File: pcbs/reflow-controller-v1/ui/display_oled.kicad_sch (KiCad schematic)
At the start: 3 parts

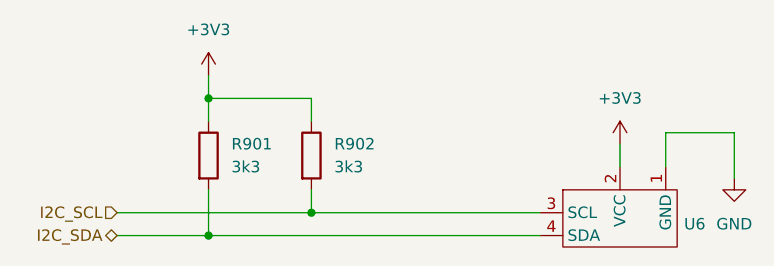
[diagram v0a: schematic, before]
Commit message: split pcbs into two for safety
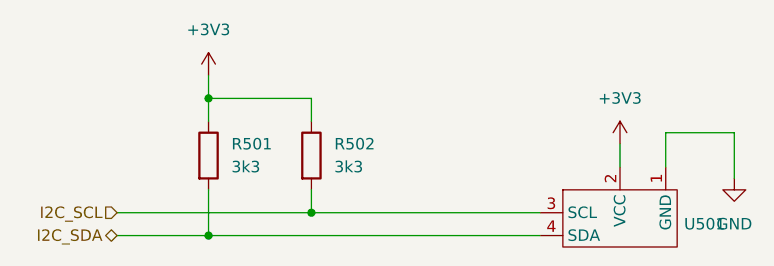
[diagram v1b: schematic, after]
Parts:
- renumbered R901 to R501, R902 to R502, U6 to U501
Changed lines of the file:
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@@
 (kicad_sch
-	(version 20231120)
+	(version 20250114)
 	(generator "eeschema")
-	(generator_version "8.0")
+	(generator_version "9.0")
 	(paper "A4")
 	(junction
@@
 		(shape input)
 		(at 91.44 88.9 180)
-		(fields_autoplaced yes)
 		(effects
 			(font
@@
 		(shape bidirectional)
 		(at 91.44 91.44 180)
-		(fields_autoplaced yes)
 		(effects
 			(font
@@
 		(dnp no)
 		(fields_autoplaced yes)
-		(property "Reference" "#PWR0903"
+		(property "Reference" "#PWR0503"
 			(at 160.02 91.44 0)
 			(effects
@@
 		)
 		(instances
-			(project "reflow-controller-v1"
-				(path "/843848ae-bf49-42cb-8f8b-76790d2e568d/28d32604-417d-4cd4-a8ef-2fae619450e6"
-					(reference "#PWR0903")
-					(unit 1)
-				)
-				(path "/843848ae-bf49-42cb-8f8b-76790d2e568d/41c2d982-496b-4922-a077-a2a7f833416c"
-					(reference "#PWR0803")
-					(unit 1)
-				)
-			)
-			(project "controller_v1"
-				(path "/c1daf800-73ea-4b6c-aa60-e9f4e3094257/1880ae86-b315-43a9-9217-9492e81597b0"
-					(reference "#PWR0403")
-					(unit 1)
-				)
-				(path "/c1daf800-73ea-4b6c-aa60-e9f4e3094257/4f03f492-0b54-42f8-83e4-aaa576a1d068"
-					(reference "#PWR0303")
-					(unit 1)
-				)
-				(path "/c1daf800-73ea-4b6c-aa60-e9f4e3094257/d31388c9-964a-4783-beb1-0c9e163732c0"
-					(reference "#PWR0203")
+			(project "ui"
+				(path "/2ced3b3e-2fc8-4776-88d1-4bcb3cd16514/6487fe46-90c2-4d94-907f-d4fbc81ee4e4"
+					(reference "#PWR0503")
+					(unit 1)
+				)
+				(path "/2ced3b3e-2fc8-4776-88d1-4bcb3cd16514/be015160-9496-4291-af46-03b91169066a"
+					(reference "#PWR0603")
 					(unit 1)
 				)
@@
 		(dnp no)
 		(fields_autoplaced yes)
-		(property "Reference" "R902"
+		(property "Reference" "R502"
 			(at 115.57 81.28 0)
 			(effects
@@
 		)
 		(instances
-			(project "reflow-controller-v1"
-				(path "/843848ae-bf49-42cb-8f8b-76790d2e568d/28d32604-417d-4cd4-a8ef-2fae619450e6"
-					(reference "R902")
-					(unit 1)
-				)
-				(path "/843848ae-bf49-42cb-8f8b-76790d2e568d/41c2d982-496b-4922-a077-a2a7f833416c"
-					(reference "R802")
-					(unit 1)
-				)
-			)
-			(project "controller_v1"
-				(path "/c1daf800-73ea-4b6c-aa60-e9f4e3094257/1880ae86-b315-43a9-9217-9492e81597b0"
-					(reference "R402")
-					(unit 1)
-				)
-				(path "/c1daf800-73ea-4b6c-aa60-e9f4e3094257/4f03f492-0b54-42f8-83e4-aaa576a1d068"
-					(reference "R302")
-					(unit 1)
-				)
-				(path "/c1daf800-73ea-4b6c-aa60-e9f4e3094257/d31388c9-964a-4783-beb1-0c9e163732c0"
-					(reference "R202")
+			(project "ui"
+				(path "/2ced3b3e-2fc8-4776-88d1-4bcb3cd16514/6487fe46-90c2-4d94-907f-d4fbc81ee4e4"
+					(reference "R502")
+					(unit 1)
+				)
+				(path "/2ced3b3e-2fc8-4776-88d1-4bcb3cd16514/be015160-9496-4291-af46-03b91169066a"
+					(reference "R602")
 					(unit 1)
 				)
@@
 		(dnp no)
 		(fields_autoplaced yes)
-		(property "Reference" "#PWR0902"
+		(property "Reference" "#PWR0502"
 			(at 147.32 85.09 0)
 			(effects
@@
 		)
 		(instances
-			(project "reflow-controller-v1"
-				(path "/843848ae-bf49-42cb-8f8b-76790d2e568d/28d32604-417d-4cd4-a8ef-2fae619450e6"
-					(reference "#PWR0902")
-					(unit 1)
-				)
-				(path "/843848ae-bf49-42cb-8f8b-76790d2e568d/41c2d982-496b-4922-a077-a2a7f833416c"
-					(reference "#PWR0802")
-					(unit 1)
-				)
-			)
-			(project "controller_v1"
-				(path "/c1daf800-73ea-4b6c-aa60-e9f4e3094257/1880ae86-b315-43a9-9217-9492e81597b0"
-					(reference "#PWR0402")
-					(unit 1)
-				)
-				(path "/c1daf800-73ea-4b6c-aa60-e9f4e3094257/4f03f492-0b54-42f8-83e4-aaa576a1d068"
-					(reference "#PWR0302")
-					(unit 1)
-				)
-				(path "/c1daf800-73ea-4b6c-aa60-e9f4e3094257/d31388c9-964a-4783-beb1-0c9e163732c0"
-					(reference "#PWR0202")
+			(project "ui"
+				(path "/2ced3b3e-2fc8-4776-88d1-4bcb3cd16514/6487fe46-90c2-4d94-907f-d4fbc81ee4e4"
+					(reference "#PWR0502")
+					(unit 1)
+				)
+				(path "/2ced3b3e-2fc8-4776-88d1-4bcb3cd16514/be015160-9496-4291-af46-03b91169066a"
+					(reference "#PWR0602")
 					(unit 1)
 				)
@@
 		(dnp no)
 		(fields_autoplaced yes)
-		(property "Reference" "#PWR0901"
+		(property "Reference" "#PWR0501"
 			(at 101.6 77.47 0)
 			(effects
@@
 		)
 		(instances
-			(project "reflow-controller-v1"
-				(path "/843848ae-bf49-42cb-8f8b-76790d2e568d/28d32604-417d-4cd4-a8ef-2fae619450e6"
-					(reference "#PWR0901")
-					(unit 1)
-				)
-				(path "/843848ae-bf49-42cb-8f8b-76790d2e568d/41c2d982-496b-4922-a077-a2a7f833416c"
-					(reference "#PWR0801")
-					(unit 1)
-				)
-			)
-			(project "controller_v1"
-				(path "/c1daf800-73ea-4b6c-aa60-e9f4e3094257/1880ae86-b315-43a9-9217-9492e81597b0"
-					(reference "#PWR0401")
-					(unit 1)
-				)
-				(path "/c1daf800-73ea-4b6c-aa60-e9f4e3094257/4f03f492-0b54-42f8-83e4-aaa576a1d068"
-					(reference "#PWR0301")
-					(unit 1)
-				)
-				(path "/c1daf800-73ea-4b6c-aa60-e9f4e3094257/d31388c9-964a-4783-beb1-0c9e163732c0"
-					(reference "#PWR0201")
+			(project "ui"
+				(path "/2ced3b3e-2fc8-4776-88d1-4bcb3cd16514/6487fe46-90c2-4d94-907f-d4fbc81ee4e4"
+					(reference "#PWR0501")
+					(unit 1)
+				)
+				(path "/2ced3b3e-2fc8-4776-88d1-4bcb3cd16514/be015160-9496-4291-af46-03b91169066a"
+					(reference "#PWR0601")
 					(unit 1)
 				)
@@
 		(on_board yes)
 		(dnp no)
-		(property "Reference" "U6"
+		(property "Reference" "U501"
 			(at 154.432 90.17 0)
 			(effects
@@
 		)
 		(instances
-			(project ""
-				(path "/843848ae-bf49-42cb-8f8b-76790d2e568d/28d32604-417d-4cd4-a8ef-2fae619450e6"
-					(reference "U6")
-					(unit 1)
-				)
-				(path "/843848ae-bf49-42cb-8f8b-76790d2e568d/41c2d982-496b-4922-a077-a2a7f833416c"
-					(reference "U5")
+			(project "ui"
+				(path "/2ced3b3e-2fc8-4776-88d1-4bcb3cd16514/6487fe46-90c2-4d94-907f-d4fbc81ee4e4"
+					(reference "U501")
+					(unit 1)
+				)
+				(path "/2ced3b3e-2fc8-4776-88d1-4bcb3cd16514/be015160-9496-4291-af46-03b91169066a"
+					(reference "U601")
 					(unit 1)
 				)
@@
 		(dnp no)
 		(fields_autoplaced yes)
-		(property "Reference" "R901"
+		(property "Reference" "R501"
 			(at 104.14 81.28 0)
 			(effects
@@
 		)
 		(instances
-			(project "reflow-controller-v1"
-				(path "/843848ae-bf49-42cb-8f8b-76790d2e568d/28d32604-417d-4cd4-a8ef-2fae619450e6"
-					(reference "R901")
-					(unit 1)
-				)
-				(path "/843848ae-bf49-42cb-8f8b-76790d2e568d/41c2d982-496b-4922-a077-a2a7f833416c"
-					(reference "R801")
-					(unit 1)
-				)
-			)
-			(project "controller_v1"
-				(path "/c1daf800-73ea-4b6c-aa60-e9f4e3094257/1880ae86-b315-43a9-9217-9492e81597b0"
-					(reference "R401")
-					(unit 1)
-				)
-				(path "/c1daf800-73ea-4b6c-aa60-e9f4e3094257/4f03f492-0b54-42f8-83e4-aaa576a1d068"
-					(reference "R301")
-					(unit 1)
-				)
-				(path "/c1daf800-73ea-4b6c-aa60-e9f4e3094257/d31388c9-964a-4783-beb1-0c9e163732c0"
-					(reference "R201")
-					(unit 1)
-				)
+			(project "ui"
+				(path "/2ced3b3e-2fc8-4776-88d1-4bcb3cd16514/6487fe46-90c2-4d94-907f-d4fbc81ee4e4"
+					(reference "R501")
+					(unit 1)
+				)
+				(path "/2ced3b3e-2fc8-4776-88d1-4bcb3cd16514/be015160-9496-4291-af46-03b91169066a"
+					(reference "R601")
+					(unit 1)
+				)
